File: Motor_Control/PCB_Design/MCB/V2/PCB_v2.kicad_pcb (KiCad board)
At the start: 2 copper layers, 34 parts, among them J1 Molex_Motor, J2 Conn_Encoder, J3 Molex_Pwr_In, J4 Teensy, J5 Molex_Pwr_Out, J6 Conn_01x07_Female, J7 PinsTeensy, J8 PinsEncoder, J9 Conn_I2C, Q1 Q_NMOS_IRLB8743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

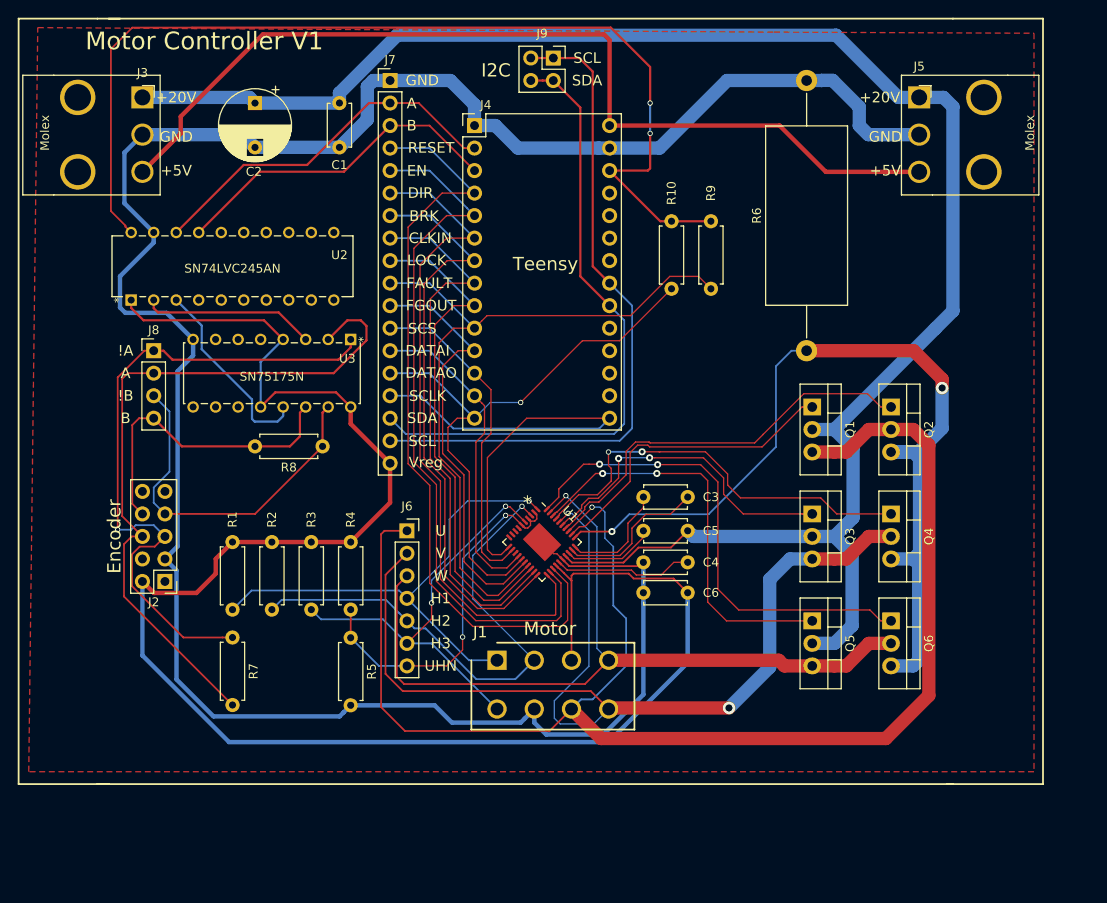
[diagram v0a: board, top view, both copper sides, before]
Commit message: Nouveau design de la board
**Pas trouvé de façon de générer une nouvelle board encore, donc repositionnement fait mais il faut arranger les tracks et tout le reste
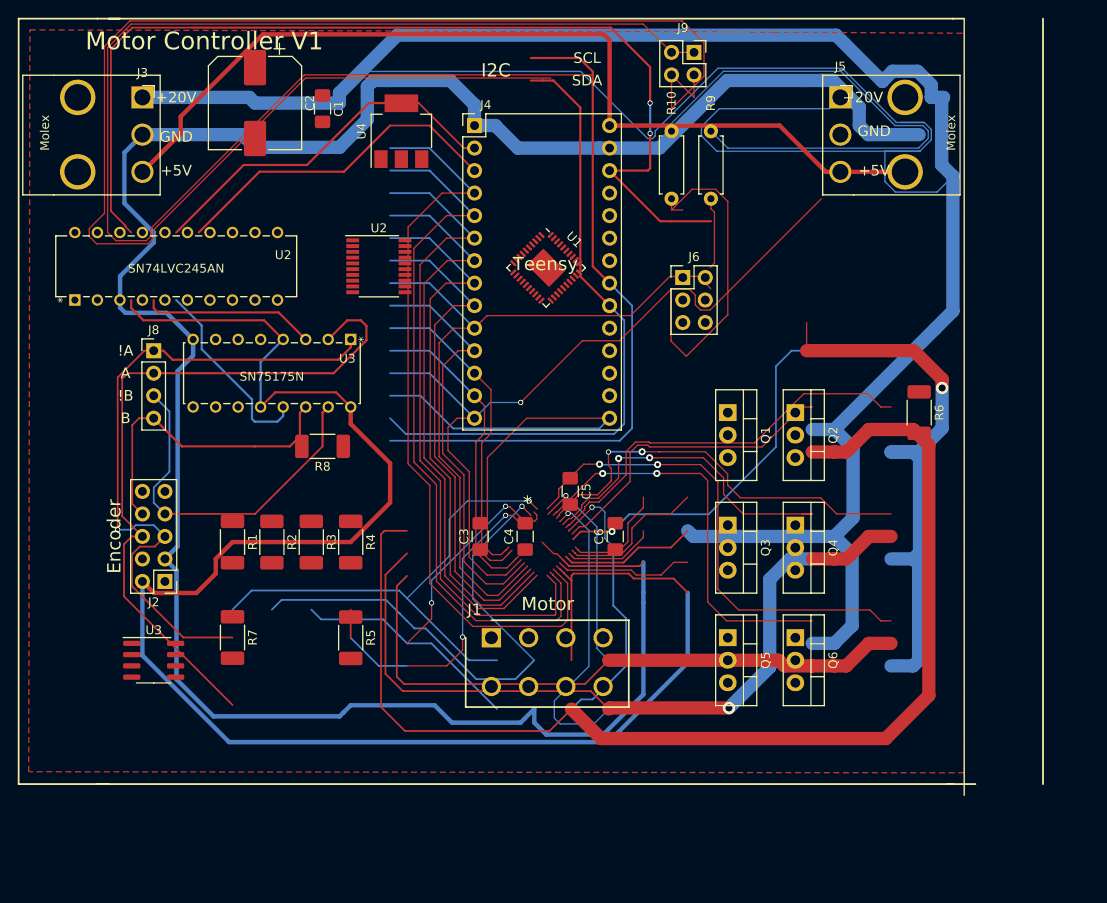
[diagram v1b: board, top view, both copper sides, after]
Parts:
- removed J7: PinsTeensy, Connector_PinHeader_2.54mm:PinHeader_1x18_P2.54mm_Vertical
- added U2: SN74LVC245APWE4, Package_SO:TSSOP-20_4.4x6.5mm_P0.65mm, F.Cu at (127.0, 77.5)
- added U3: SN65LVDT34D-MyLibrary, Package_SO:SOIC-8_3.9x4.9mm_P1.27mm, F.Cu at (101.6, 121.9)
- added U4: LM2931, Package_TO_SOT_SMD:SOT-223-3_TabPin2, F.Cu at (129.5, 62.2)
- C1, C3, C4, C5, C6: footprint Capacitor_THT:C_Disc_D4.7mm_W2.5mm_P5.00mm -> Capacitor_SMD:C_1206_3216Metric_Pad1.42x1.75mm_HandSolder
- C2: footprint Capacitor_THT:CP_Radial_D8.0mm_P5.00mm -> Capacitor_SMD:CP_Elec_10x10
- J6: value Conn_01x07_Female -> Adress_Pins; footprint Connector_PinSocket_2.54mm:PinSocket_1x07_P2.54mm_Vertical -> Connector_PinHeader_2.54mm:PinHeader_2x03_P2.54mm_Vertical
- R1, R2, R3, R4, R5, R7, R8: footprint Resistor_THT:R_Axial_DIN0207_L6.3mm_D2.5mm_P7.62mm_Horizontal -> Resistor_SMD:R_2010_5025Metric_Pad1.52x2.65mm_HandSolder
- R6: footprint Resistor_THT:R_Axial_DIN0922_L20.0mm_D9.0mm_P30.48mm_Horizontal -> Resistor_SMD:R_2010_5025Metric_Pad1.52x2.65mm_HandSolder
- moved J6 42.2 mm to (161.3, 78.7)
- moved U1 30.9 mm to (145.9, 77.6)
- moved C3 18.9 mm to (138.4, 108.0), turned to 90 degrees
- moved J9 15.9 mm to (162.6, 53.3)
- moved R6 14.5 mm to (188.0, 94.0), turned to 270 degrees
- moved C5 14.0 mm to (148.6, 102.9), turned to 270 degrees
- moved C4 13.7 mm to (143.5, 108.0), turned to 90 degrees
- moved Q6 11.0 mm to (174.0, 119.4)
- moved Q4 10.9 mm to (174.0, 106.7)
- moved Q2 10.8 mm to (174.0, 94.0)
- moved R10 10.2 mm to (160.0, 69.8)
- moved R9 10.2 mm to (164.5, 69.8)
- moved Q5 9.71 mm to (166.4, 119.4)
- moved Q3 9.61 mm to (166.4, 106.7)
- moved Q1 9.55 mm to (166.4, 94.0)
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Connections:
- net /MCU/A7 renamed /LED3
- net /MCU/A8 renamed /LED2
- net /MCU/A9 renamed /LED1
- C1 pad 1: /Vm -> /Vm_in
- C2 pad 1: /Vm -> /Vm_in
- J1 pad 1: /Hall_1 -> /Hall_3
- J1 pad 2: /Hall_2 -> GNDREF
- J1 pad 3: /Vreg -> Motor_1
- J1 pad 4: Motor_3 -> Motor_2
- J1 pad 5: /Hall_3 -> /Hall_1
- J1 pad 6: GNDREF -> /Hall_2
- J1 pad 7: Motor_1 -> /Vreg
- J1 pad 8: Motor_2 -> Motor_3
- J2 pad 10: Net-(J2-Pad10) -> /Vreg
- J2 pad 2: /Vreg -> Net-(J2-Pad2)
- J2 pad 3: GNDREF -> /ENC_!B
- J2 pad 4: Net-(J2-Pad4) -> /ENC_B
- J2 pad 7: /ENC_!B -> GNDREF
- J2 pad 8: /ENC_B -> Net-(J2-Pad8)
- J3 pad 1: /Vm -> /Vm_in
- J3 pad 3: /Vin -> Net-(J3-Pad3)
- J5 pad 1: /Vm -> /Vm_in
- J5 pad 3: /Vin -> Net-(J5-Pad3)
- J6 pad 1: Motor_1 -> /MCU/A0
- J6 pad 2: Motor_2 -> GNDREF
- J6 pad 3: Motor_3 -> /MCU/A1
- J6 pad 4: /Hall_1 -> GNDREF
- J6 pad 5: /Hall_2 -> /MCU/A2
- J6 pad 6: /Hall_3 -> GNDREF
- R7 pad 1: /ENC_!A -> /ENC_!B
- R7 pad 2: /ENC_A -> /ENC_B
- R8 pad 1: /ENC_!B -> /ENC_A
- R8 pad 2: /ENC_B -> /ENC_!A
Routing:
- net /Vm_in: track 0.00 -> 335.2 mm
- net GNDREF: track 266.2 -> 501.3 mm, vias 0 -> 2
- net /SDA: track 72.2 -> 243.8 mm
- net /SCL: track 77.6 -> 230.4 mm
- net Motor_1: track 165.1 -> 26.0 mm, vias 1 -> 0
- net Motor_2: track 121.5 -> 9.94 mm, vias 2 -> 0
- net /Vm: track 205.7 -> 94.9 mm, vias 0 -> 3
- net /Vreg: track 197.6 -> 290.6 mm, vias 0 -> 5
- net Net-(C4-Pad2): track 15.6 -> 79.3 mm, vias 0 -> 4
- net /DATAO: track 66.4 -> 128.3 mm
- net /3.3V: track 115.2 -> 176.7 mm
- net /Power/WLSG: track 55.9 -> 0.00 mm, vias 2 -> 0
- net Motor_3: track 93.9 -> 147.6 mm
- net /Power/VLSG: track 47.0 -> 0.00 mm, vias 2 -> 0
- net /Power/VHSG: track 37.7 -> 0.00 mm, vias 2 -> 0
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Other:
- board text removed: "BRK"
- board text removed: "CLKIN"
- board text removed: "DATAI"
- board text removed: "DATAO"
- board text removed: "DIR"
- board text removed: "EN"
- board text removed: "FAULT"
- board text removed: "FGOUT"
- board text removed: "H1"
- board text removed: "H2"
- board text removed: "H3"
- board text removed: "LOCK"
- board text removed: "RESET"
- board text removed: "SCLK"
- board text removed: "SCS"
- board text removed: "U"
- board text removed: "UHN"
- board text removed: "V"
- board text removed: "Vreg"
- board text removed: "W"

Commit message: Début de la nouvelle board
Les molex, teensy et autres ne loadent pas sur mon ordi
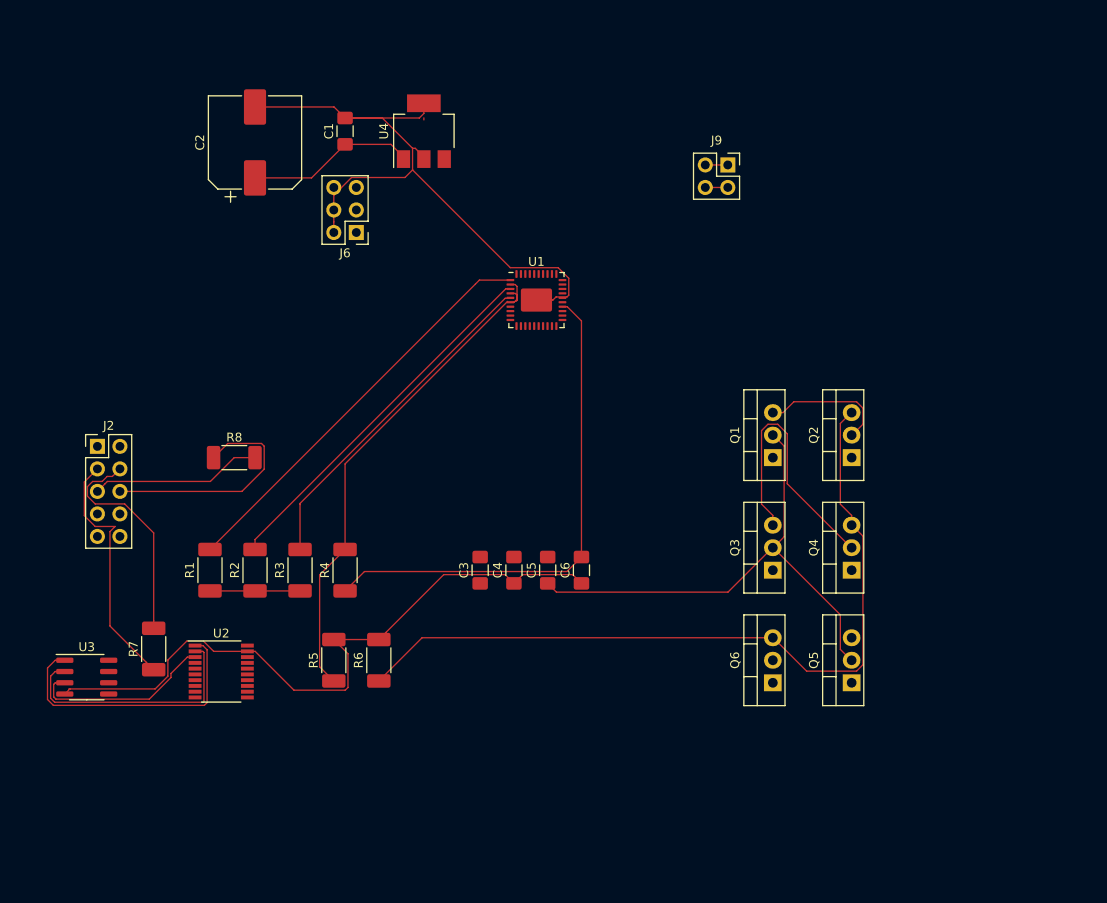
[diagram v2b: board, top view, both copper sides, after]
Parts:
- removed J1: Molex_Motor, 39-28-1083:SHDR8W125P550X420_2X4_1800X960X1310P
- removed J3: Molex_Pwr_In, MyLibrary:Molex,1x3
- removed J4: Teensy, MyLibrary:TeensyLC
- removed J5: Molex_Pwr_Out, MyLibrary:Molex,1x3,Right
- removed J8: PinsEncoder, Connector_PinHeader_2.54mm:PinHeader_1x04_P2.54mm_Vertical
- removed R10, R9: 4.7k, Resistor_THT:R_Axial_DIN0207_L6.3mm_D2.5mm_P7.62mm_Horizontal
- removed the U2 at (127.0, 77.5)
- removed the U2 at (115.6, 73.7)
- removed the U3 at (101.6, 121.9)
- removed the U3 at (106.0, 93.3)
- added U2: SN74LVC245APWE4, Package_SO:TSSOP-20_4.4x6.5mm_P0.65mm, F.Cu at (109.2, 123.2)
- added U3: SN65LVDT34D-MyLibrary, Package_SO:SOIC-8_3.9x4.9mm_P1.27mm, F.Cu at (94.0, 123.8)
- moved R6 67.1 mm to (127.0, 121.9), turned to 90 degrees
- moved J6 37.2 mm to (124.5, 73.7), turned to 180 degrees
- moved J2 17.0 mm to (95.2, 97.8), turned to 0 degrees
- moved Q5 14.9 mm to (180.3, 124.5), turned to 90 degrees
- moved J9 13.3 mm to (166.4, 66.0)
- moved R8 10.0 mm to (110.7, 99.1), turned to 0 degrees
- moved C5 9.25 mm to (146.1, 111.8), turned to 90 degrees
- moved R7 8.98 mm to (101.6, 120.7), turned to 90 degrees
- moved Q2 8.13 mm to (180.3, 99.1), turned to 90 degrees
- moved Q4 8.13 mm to (180.3, 111.8), turned to 90 degrees
- moved Q1 7.18 mm to (171.4, 99.1), turned to 90 degrees
- moved Q3 7.18 mm to (171.4, 111.8), turned to 90 degrees
- moved Q6 5.68 mm to (171.4, 124.5), turned to 90 degrees
- moved C6 5.39 mm to (149.9, 111.8)
- moved C2 4.45 mm to (113.0, 63.5), turned to 90 degrees
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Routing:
- net GNDREF: track 501.3 -> 153.4 mm, vias 2 -> 0
- net /Vm_in: track 335.2 -> 19.2 mm
- net /SDA: track 243.8 -> 2.54 mm
- net /SCL: track 230.4 -> 2.54 mm
- net /Vreg: track 290.6 -> 99.6 mm, vias 5 -> 0
- net /3.3V: track 176.7 -> 0.00 mm, vias 2 -> 0
- net Motor_3: track 147.6 -> 0.00 mm, vias 1 -> 0
- net /DATAO: track 128.3 -> 0.00 mm, vias 1 -> 0
- net /Vin: track 107.3 -> 0.00 mm
- net /FAULTn: track 90.8 -> 0.00 mm
- net /RESET: track 86.2 -> 0.00 mm
- net /Power/ULSG: track 80.5 -> 0.00 mm
- net /ENABLE: track 80.2 -> 0.00 mm
- net Net-(C4-Pad2): track 79.3 -> 0.00 mm, vias 4 -> 0
- net /DIR: track 75.0 -> 0.00 mm
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- removed copper zone on F.Cu, net GNDREF
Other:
- board text removed: "!A"
- board text removed: "!B"
- board text removed: "*"
- board text removed: "+20V"
- board text removed: "+5V"
- board text removed: "A"
- board text removed: "B"
- board text removed: "Encoder"
- board text removed: "GND"
- board text removed: "I2C"
- board text removed: "Motor"
- board text removed: "Motor Controller V1"
- board text removed: "SCL"
- board text removed: "SDA"
- board text removed: "Teensy"

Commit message: Pcb
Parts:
- added J1: Molex_Motor, 39-28-1083:SHDR8W125P550X420_2X4_1800X960X1310P, F.Cu at (134.3, 125.6)
- added J3: Molex_Pwr_In, MyLibrary:Molex,1x3, F.Cu at (144.7, 136.3)
- added J4: Teensy, MyLibrary:TeensyLC, F.Cu at (132.9, 83.7)
- added J5: Molex_Pwr_Out, MyLibrary:Molex,1x3,Right, F.Cu at (152.1, 125.9)
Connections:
- C1 pad 1: /Vm_in -> /Vm
- C2 pad 1: /Vm_in -> /Vm
- U4 pad 1: /Vm_in -> /Vm
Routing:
- net /Vm: track 58.1 -> 77.2 mm
- net /Vm_in: track 19.2 -> 0.00 mm

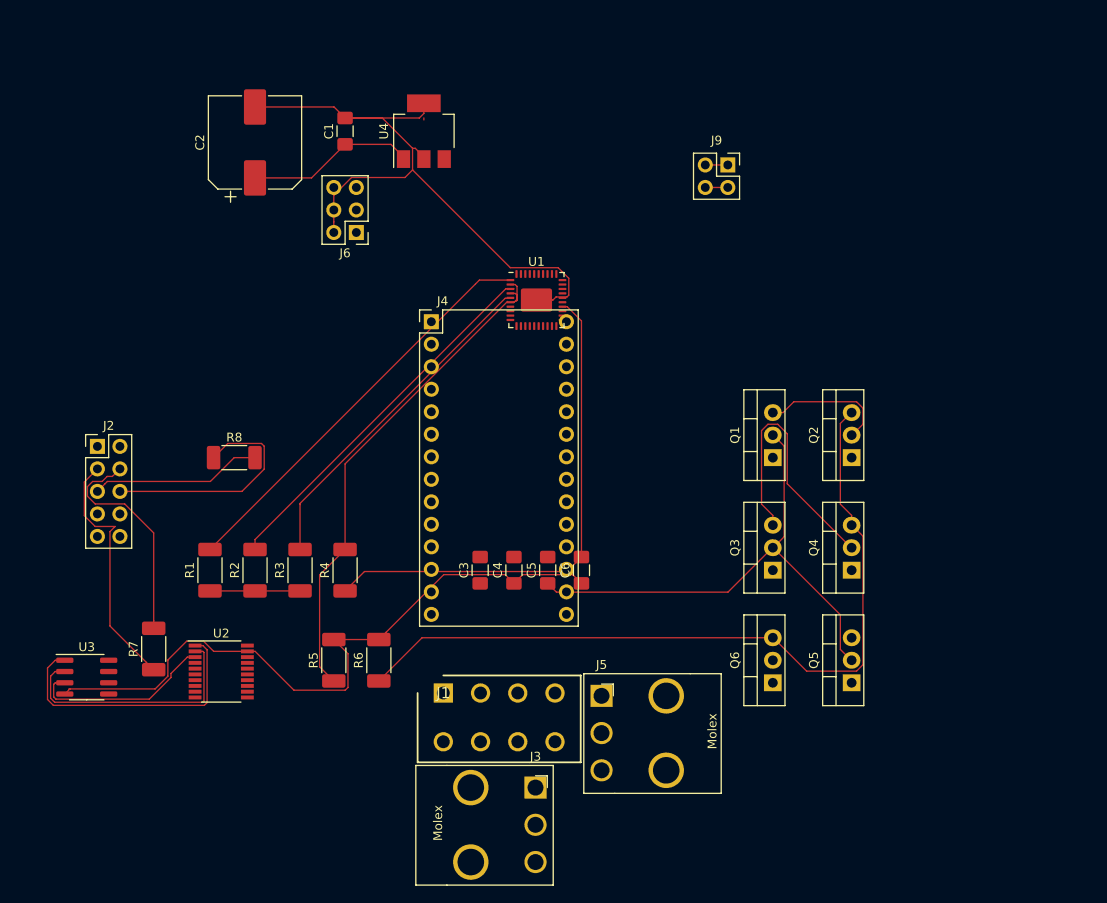
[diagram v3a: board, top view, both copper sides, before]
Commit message: PCB à jour, track manquante
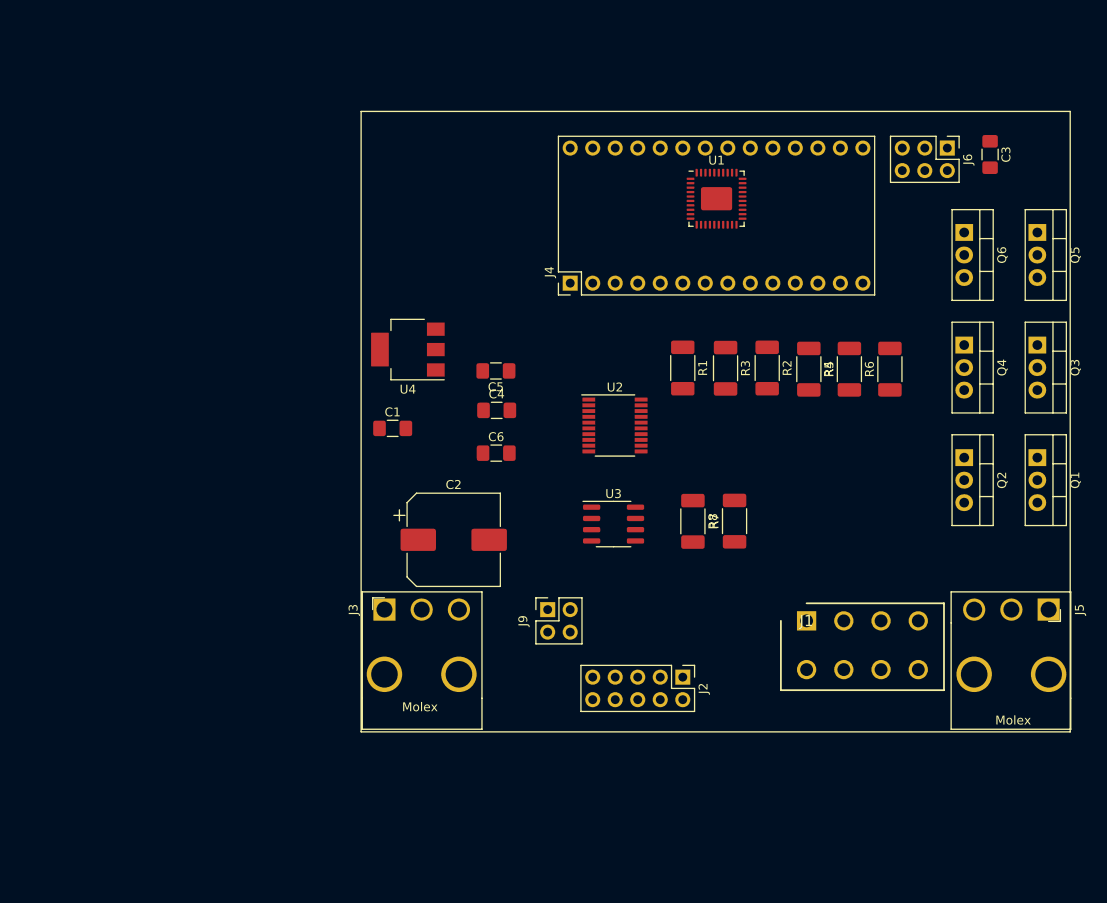
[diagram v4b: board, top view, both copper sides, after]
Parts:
- moved C3 74.2 mm to (196.0, 64.9), turned to 270 degrees
- moved J2 71.0 mm to (161.3, 123.8), turned to 270 degrees
- moved J6 67.4 mm to (191.1, 64.1), turned to 270 degrees
- moved R7 67.1 mm to (167.1, 106.2)
- moved R5 66.8 mm to (180.1, 89.1)
- moved R6 66.4 mm to (184.7, 89.1)
- moved R2 62.1 mm to (170.8, 89.0), turned to 270 degrees
- moved U3 61.9 mm to (153.5, 106.6)
- moved R1 58.0 mm to (161.3, 89.0), turned to 270 degrees
- moved R4 57.0 mm to (175.5, 89.1), turned to 270 degrees
- moved Q6 55.2 mm to (193.0, 73.7), turned to 270 degrees
- moved Q5 55.0 mm to (201.3, 73.7), turned to 270 degrees
- moved J9 54.1 mm to (146.1, 116.2), turned to 90 degrees
- moved R3 53.1 mm to (166.1, 89.0), turned to 270 degrees
- moved U2 52.4 mm to (153.6, 95.4)
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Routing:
- net GNDREF: track 153.4 -> 0.00 mm
- net /Vreg: track 99.6 -> 0.00 mm
- net /Power/ISEN: track 88.6 -> 0.00 mm
- net /Vm: track 77.2 -> 0.00 mm
- net /UHN: track 57.0 -> 0.00 mm
- net /Hall_1: track 46.5 -> 0.00 mm
- net /Hall_2: track 42.0 -> 0.00 mm
- net /Hall_3: track 38.9 -> 0.00 mm
- net Motor_2: track 30.7 -> 0.00 mm
- net Net-(U2-Pad2): track 28.4 -> 0.00 mm
- net /ENC_!B: track 28.3 -> 0.00 mm
- net /ENC_A: track 26.4 -> 0.00 mm
- net /ENC_B: track 25.5 -> 0.00 mm
- net Net-(U2-Pad3): track 21.0 -> 0.00 mm
- net /ENC_!A: track 19.4 -> 0.00 mm
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
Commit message: PBC avec groundplane et labels placés, tracks manquantes
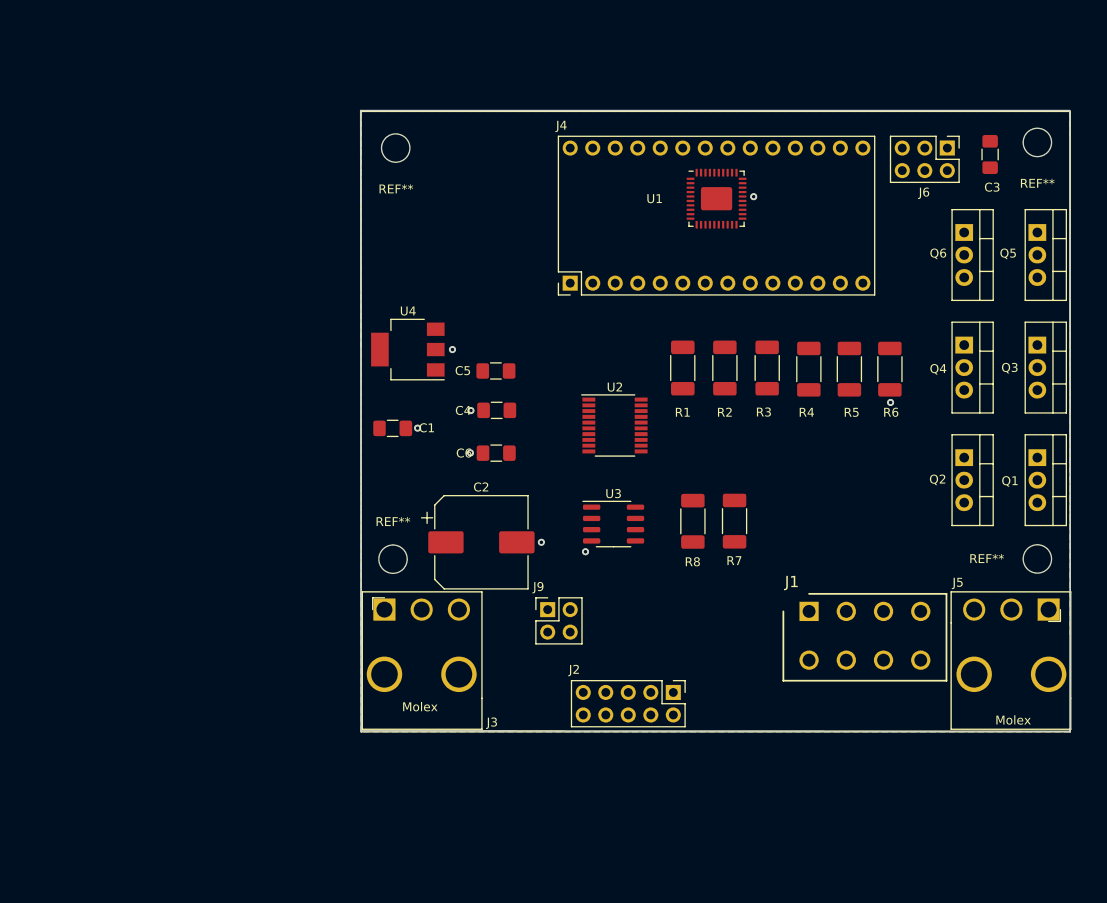
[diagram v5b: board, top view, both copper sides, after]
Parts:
- added REF**: MountingHole_3.2mm_M3, MountingHole:MountingHole_3.2mm_M3, F.Cu at (201.3, 63.5)
- added REF**: MountingHole_3.2mm_M3, MountingHole:MountingHole_3.2mm_M3, F.Cu at (128.9, 64.1)
- added REF**: MountingHole_3.2mm_M3, MountingHole:MountingHole_3.2mm_M3, F.Cu at (128.6, 110.5)
- added REF**: MountingHole_3.2mm_M3, MountingHole:MountingHole_3.2mm_M3, F.Cu at (201.3, 110.5)
- moved R2 4.78 mm to (166.0, 89.0)
- moved R3 4.70 mm to (170.8, 89.0)
- moved C2 3.14 mm to (138.6, 108.6)
- moved J2 2.03 mm to (160.2, 125.6)
- moved J1 1.10 mm to (175.5, 116.4)
- turned R5 to 270 degrees
- turned R6 to 270 degrees
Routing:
- net GNDREF: vias 0 -> 8
- added copper zone on B.Cu, net GNDREF
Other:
- board outline added: 80.1 x 70 mm
